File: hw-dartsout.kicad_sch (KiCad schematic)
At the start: 44 parts, among them J1 Conn_01x10_Socket, J2 Conn_01x10_Socket, J3 Conn_01x02_Pin, SW1 SW_Push, U1 ESP32-S3-WROOM-1, U3 NCP1117-3.3_SOT223

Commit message: First draft placement and layout
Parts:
- added J4: Conn_01x04_Pin, Connector_PinHeader_2.54mm:PinHeader_1x04_P2.54mm_Vertical, symbol Connector:Conn_01x04_Pin
- JP2: footprint Capacitor_SMD:C_0603_1608Metric -> Jumper:SolderJumper-3_P1.3mm_Bridged12_RoundedPad1.0x1.5mm
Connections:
- net +3V3: now also J4.1 (Pin_1)
- net ESP_RX: now also J4.3 (Pin_3)
- net ESP_TX: now also J4.2 (Pin_2)
- net GND: now also J4.4 (Pin_4)
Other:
- note added: "Add testpoints / leds WROOM or SOLO?? Office stock!"
- note removed: "Add testpoints / leds"
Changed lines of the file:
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@@
+    (stroke (width 0) (type default))
+  )
+  (wire (pts (xy 252.73 140.97) (xy 243.84 140.97))
     (stroke (width 0) (type default))
   )
@@
     (stroke (width 0) (type default))
   )
+  (wire (pts (xy 252.73 138.43) (xy 243.84 138.43))
+    (stroke (width 0) (type default))
+  )
   (wire (pts (xy 125.73 104.14) (xy 134.62 104.14))
     (stroke (width 0) (type default))
@@
     (stroke (width 0) (type default))
   )
+  (wire (pts (xy 254 143.51) (xy 243.84 143.51))
+    (stroke (width 0) (type default))
+  )
   (wire (pts (xy 134.62 73.66) (xy 125.73 73.66))
     (stroke (width 0) (type default))
@@
     (stroke (width 0) (type default))
   )
+  (wire (pts (xy 254 135.89) (xy 243.84 135.89))
+    (stroke (width 0) (type default))
+  )
   (wire (pts (xy 125.73 83.82) (xy 134.62 83.82))
     (stroke (width 0) (type default))
@@
     (effects (font (size 1.27 1.27)) (justify left bottom))
   )
-  (text "Add testpoints / leds" (at 176.53 170.18 0)
+  (text "Add testpoints / leds\nWROOM or SOLO?? Office stock!"
+    (at 179.07 172.72 0)
     (effects (font (size 1.27 1.27)) (justify left bottom))
   )
@@
     (effects (font (size 1.27 1.27)) (justify left bottom))
   )
+  (label "ESP_TX" (at 252.73 138.43 180) (fields_autoplaced)
+    (effects (font (size 1.27 1.27)) (justify right bottom))
+  )
   (label "ROW_10" (at 134.62 99.06 180) (fields_autoplaced)
     (effects (font (size 1.27 1.27)) (justify right bottom))
@@
   (label "ROW_05" (at 236.22 64.77 0) (fields_autoplaced)
     (effects (font (size 1.27 1.27)) (justify left bottom))
+  )
+  (label "ESP_RX" (at 252.73 140.97 180) (fields_autoplaced)
+    (effects (font (size 1.27 1.27)) (justify right bottom))
   )
   (label "ROW_07" (at 236.22 59.69 0) (fields_autoplaced)
@@
     )
   )
+  (symbol (lib_id "power:GND") (at 254 143.51 90) (unit 1)
+    (in_bom yes) (on_board yes) (dnp no) (fields_autoplaced)
+    (property "Reference" "#PWR018" (at 260.35 143.51 0)
+      (effects (font (size 1.27 1.27)) hide)
+    )
+    (property "Value" "GND" (at 257.81 143.51 90)
+      (effects (font (size 1.27 1.27)) (justify right))
+    )
+    (property "Footprint" "" (at 254 143.51 0)
+      (effects (font (size 1.27 1.27)) hide)
+    )
+    (property "Datasheet" "" (at 254 143.51 0)
+      (effects (font (size 1.27 1.27)) hide)
+    )
+    (pin "1")
+    (instances
+      (project "hw-dartsout"
+        (path "/c7fe45ce-d299-4ee8-a474-c3e52ad7951d"
+          (reference "#PWR018") (unit 1)
+        )
+      )
+    )
+  )
   (symbol (lib_id "Device:R") (at 198.12 83.82 0) (unit 1)
     (in_bom yes) (on_board yes) (dnp no)
@@
       (effects (font (size 1.27 1.27)))
     )
-    (property "Footprint" "Capacitor_SMD:C_0603_1608Metric" (at 260.35 99.06 0)
+    (property "Footprint" "Jumper:SolderJumper-3_P1.3mm_Bridged12_RoundedPad1.0x1.5mm" (at 260.35 99.06 0)
       (effects (font (size 1.27 1.27)) hide)
     )
@@
     )
   )
+  (symbol (lib_id "Connector:Conn_01x04_Pin") (at 238.76 138.43 0) (unit 1)
+    (in_bom yes) (on_board yes) (dnp no) (fields_autoplaced)
+    (property "Reference" "J4" (at 239.395 130.81 0)
+      (effects (font (size 1.27 1.27)))
+    )
+    (property "Value" "Conn_01x04_Pin" (at 239.395 133.35 0)
+      (effects (font (size 1.27 1.27)))
+    )
+    (property "Footprint" "Connector_PinHeader_2.54mm:PinHeader_1x04_P2.54mm_Vertical" (at 238.76 138.43 0)
+      (effects (font (size 1.27 1.27)) hide)
+    )
+    (property "Datasheet" "~" (at 238.76 138.43 0)
+      (effects (font (size 1.27 1.27)) hide)
+    )
+    (pin "4")
+    (pin "3")
+    (pin "2")
+    (pin "1")
+    (instances
+      (project "hw-dartsout"
+        (path "/c7fe45ce-d299-4ee8-a474-c3e52ad7951d"
+          (reference "J4") (unit 1)
+        )
+      )
+    )
+  )
   (symbol (lib_id "power:+5V") (at 50.8 167.64 0) (unit 1)
     (in_bom yes) (on_board yes) (dnp no)
@@
         )
       )
+    )
+  )
+  (symbol (lib_id "power:+3V3") (at 254 135.89 270) (unit 1)
+    (in_bom yes) (on_board yes) (dnp no) (fields_autoplaced)
+    (property "Reference" "#PWR019" (at 250.19 135.89 0)
+      (effects (font (size 1.27 1.27)) hide)
+    )
+    (property "Value" "+3V3" (at 257.81 135.89 90)
+      (effects (font (size 1.27 1.27)) (justify left))
+    )
+    (property "Footprint" "" (at 254 135.89 0)
+      (effects (font (size 1.27 1.27)) hide)
+    )
+    (property "Datasheet" "" (at 254 135.89 0)
+      (effects (font (size 1.27 1.27)) hide)
+    )
+    (pin "1")
+    (instances
+      (project "hw-dartsout"
+        (path "/c7fe45ce-d299-4ee8-a474-c3e52ad7951d"
+          (reference "#PWR019") (unit 1)
+        )
+      )

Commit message: PCB routed
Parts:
- removed TP2, TP3: TestPoint, TestPoint:TestPoint_Pad_D1.5mm, symbol Connector:TestPoint
- removed U1: ESP32-S3-WROOM-1, PCM_Espressif:ESP32-S3-WROOM-1, symbol PCM_Espressif:ESP32-S3-WROOM-1
- added J5, J6: Conn_01x10_Socket, Connector_PinSocket_2.54mm:PinSocket_1x10_P2.54mm_Vertical, symbol Connector:Conn_01x10_Socket
- added TP6: TestPoint, TestPoint:TestPoint_Pad_D1.5mm, symbol Connector:TestPoint
- added U1: ESP32-S2-SOLO, PCM_Espressif:ESP32-S2-SOLO, symbol guille-lib:ESP32-S2-SOLO
- H1, H2, H3, H4: footprint MountingHole:MountingHole_3.2mm_M3_Pad_TopBottom -> MountingHole:MountingHole_3.2mm_M3_DIN965_Pad_TopBottom
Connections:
- net +3V3: now also U1.2 (3V3)
- net COL_01: now also J5.1 (Pin_1), U1.30 (SPIDQS/GPIO37/FSPIQ)
- net COL_02: now also J5.2 (Pin_2), U1.29 (SPIIO7/GPIO36/FSPICLK)
- net COL_03: now also J5.3 (Pin_3), U1.28 (SPIIO6/GPIO35/FSPID)
- net COL_04: now also J5.4 (Pin_4), U1.25 (SPIIO5/GPIO34/FSPICS0)
- net COL_05: now also J5.5 (Pin_5), U1.24 (SPIIO4/GPIO33/FSPIHD)
- net COL_06: now also J5.6 (Pin_6), U1.23 (GPIO21)
- net COL_07: now also J5.7 (Pin_7), U1.22 (GPIO14/TOUCH14/ADC2_CH3/FSPIWP/FSPIDQS)
- net COL_08: now also J5.8 (Pin_8), U1.21 (GPIO13/TOUCH13/ADC2_CH2/FSPIQ/FSPIIO7)
- net COL_09: now also J5.9 (Pin_9), U1.20 (GPIO12/TOUCH12/ADC2_CH1/FSPICLK/FSPIIO6)
- net COL_10: now also J5.10 (Pin_10), U1.19 (GPIO11/TOUCH11/ADC2_CH0/FSPID/FSPIIO5)
- net ESP_IO0: now also U1.27 (GPIO0)
- net ESP_RX: now also U1.36 (U0RXD/GPIO44/CLK_OUT2)
- net ESP_TX: now also U1.37 (U0TXD/GPIO43/CLK_OUT1)
- net GND: now also U1.1 (GND), U1.40 (GND), U1.41 (GND)
- net ROW_01: now also J6.1 (Pin_1), U1.18 (GPIO10/TOUCH10/ADC1_CH9/FSPICS0/FSPIIO4)
- net ROW_02: now also J6.2 (Pin_2), U1.17 (GPIO9/TOUCH9/ADC1_CH8/FSPIHD)
- net ROW_03: now also J6.3 (Pin_3), U1.15 (GPIO3/TOUCH3/ADC1_CH2)
- net ROW_04: now also J6.4 (Pin_4), U1.12 (GPIO8/TOUCH8/ADC1_CH7)
- net ROW_05: now also J6.5 (Pin_5), U1.11 (GPIO18/U1RXD/ADC2_CH7/DAC_2/CLK_OUT3)
- net ROW_06: now also J6.6 (Pin_6), U1.10 (GPIO17/U1TXD/ADC2_CH6/DAC_1)
- net ROW_07: now also J6.7 (Pin_7), U1.7 (GPIO7/TOUCH7/ADC1_CH6)
- net ROW_08: now also J6.8 (Pin_8), U1.6 (GPIO6/TOUCH6/ADC1_CH5)
- net ROW_09: now also J6.9 (Pin_9), U1.5 (GPIO5/TOUCH5/ADC1_CH4)
- net ROW_10: now also J6.10 (Pin_10), U1.4 (GPIO4/TOUCH4/ADC1_CH3)
- net at TP5.1: now also U1.16 (GPIO46)
- net at TP4.1: now also U1.38 (GPIO2/TOUCH2/ADC1_CH1)
- net at C5.1, R21.2: now also U1.3 (EN)
- net at TP1.1: now also U1.39 (GPIO1/TOUCH1/ADC1_CH0)
- new net: TP6.1, U1.31 (GPIO38/FSPIWP)
- no-connect marks 12 -> 13
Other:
- note added: "Add testpoints / leds WROOM or SOLO?? Office stock! Separar headers (ocupan 1 hole de mas, separar 2.54*3) En prototipo, están separados 2.54 * 8"
- note removed: "Add testpoints / leds WROOM or SOLO?? Office stock!"
- moved on the sheet: C5, J1, J2, JP1, JP2, R1, R10, R11, R12, R13, R14, R15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

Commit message: Finish route, serigrphy and checks
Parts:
- added D1, D2, D3: LED, LED_SMD:LED_0603_1608Metric, symbol Device:LED
- added R23, R24, R25: 1k, Resistor_SMD:R_0603_1608Metric, symbol Device:R
- R1, R10, R11, R12, R13, R14, R15, R16, R17, R18, R19, R2, R20, R3, R4, R5, R6, R7, R8, R9: value R -> 10k
- renumbered C4 to C3, C3 to C4, H2 to H1, H1 to H2, TP5 to TP1, TP1 to TP2, TP6 to TP3, U3 to U2
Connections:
- net +3V3: now also D1.2 (A)
- net GND: now also R23.2, R24.2, R25.2
- net LED2: now reaches TP4.1, U1.38 (GPIO2/TOUCH2/ADC1_CH1)
- net LED2: now also D3.2 (A)
- net LED1: now reaches TP2.1, U1.39 (GPIO1/TOUCH1/ADC1_CH0)
- net LED1: now also D2.2 (A)
- new net: D3.1 (K), R25.1
- new net: D2.1 (K), R24.1
- new net: D1.1 (K), R23.1
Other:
- moved on the sheet: C1, C2, C3, C4, C5, H1, H2, H3, H4, J3, J4, R21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

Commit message: Revision 0.1
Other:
- note removed: "Add testpoints / leds WROOM or SOLO?? Office stock! Separar headers (ocupan 1 hole de mas, separar 2.54*3) En prototipo, están separados 2.54 * 8"
- company: (none) -> Guille González
- title: (none) -> Dartsout
- moved on the sheet: D1, D2, D3, H1, H2, H3, H4, J1, J2, J4, J5, J6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

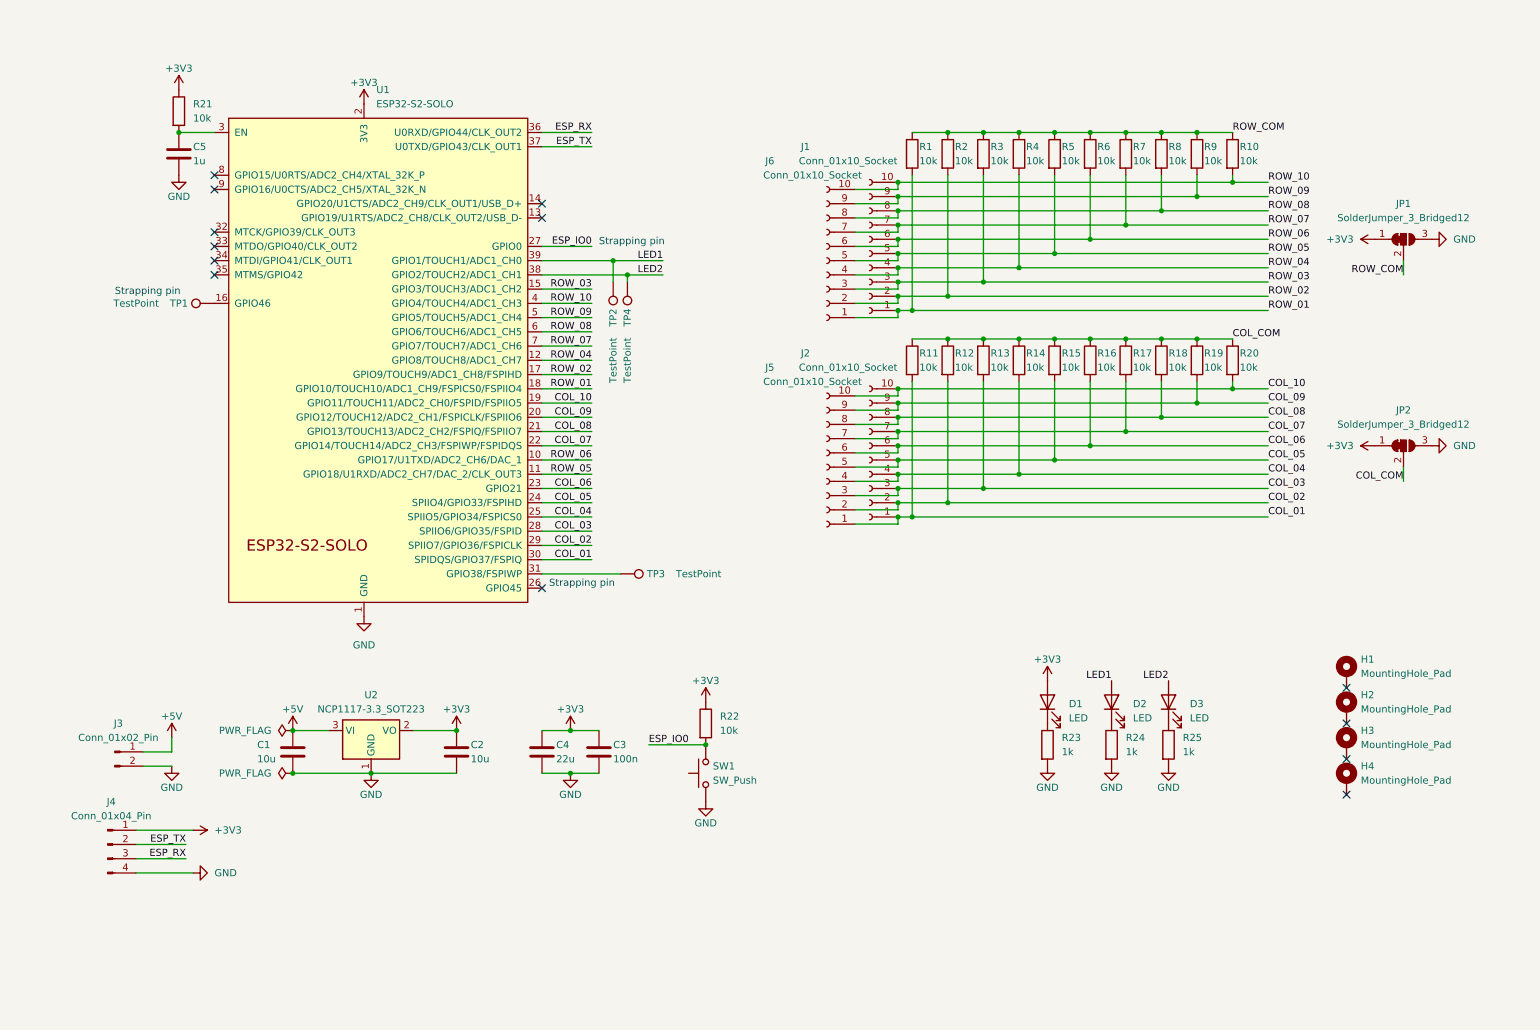
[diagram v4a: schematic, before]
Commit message: Changed sch and start with layout for next version
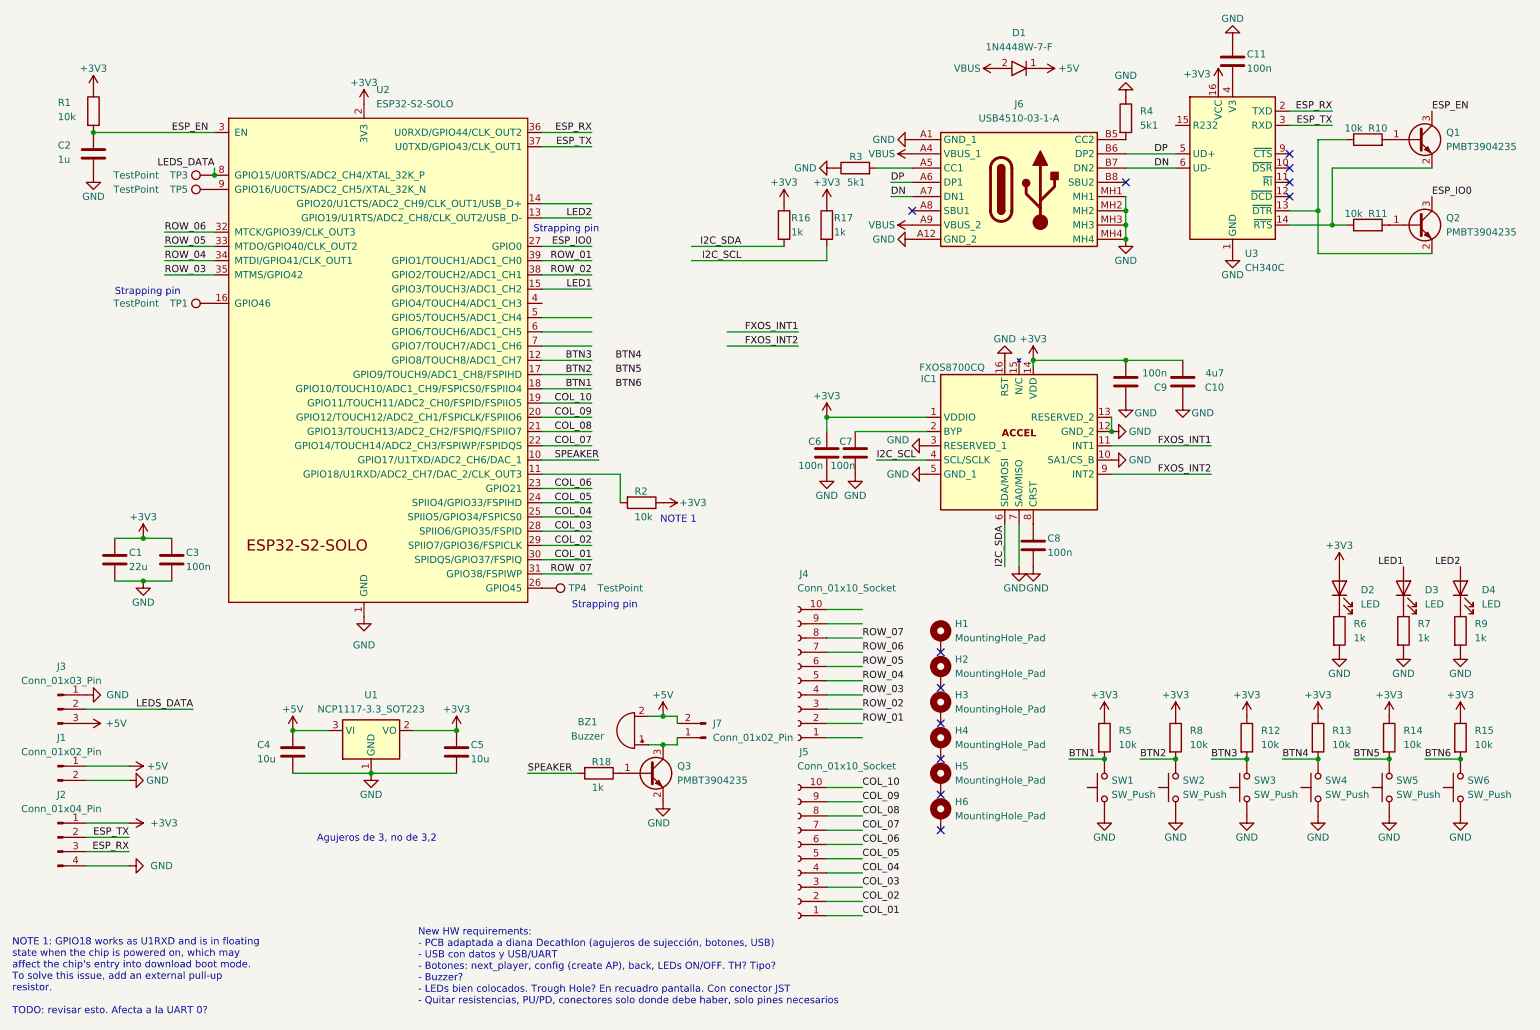
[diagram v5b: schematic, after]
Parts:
- removed J4: Conn_01x04_Pin, Connector_PinHeader_2.54mm:PinHeader_1x04_P2.54mm_Vertical, symbol Connector:Conn_01x04_Pin
- removed J5, J6: Conn_01x10_Socket, Connector_PinSocket_2.54mm:PinSocket_1x10_P2.54mm_Vertical, symbol Connector:Conn_01x10_Socket
- removed JP1, JP2: SolderJumper_3_Bridged12, Jumper:SolderJumper-3_P1.3mm_Bridged12_RoundedPad1.0x1.5mm, symbol Jumper:SolderJumper_3_Bridged12
- removed R1, R19, R20, R22, R6, R7, R9: 10k, Resistor_SMD:R_0603_1608Metric, symbol Device:R
- removed TP2: TestPoint, TestPoint:TestPoint_Pad_D1.5mm, symbol Connector:TestPoint
- added BZ1: Buzzer, Buzzer_Beeper:Buzzer_12x9.5RM7.6, symbol Device:Buzzer
- added C10: 4u7, Capacitor_SMD:C_0805_2012Metric, symbol Device:C
- added C11, C6, C7, C8, C9: 100n, Capacitor_SMD:C_0603_1608Metric, symbol Device:C
- added D1: 1N4448W-7-F, Diode_SMD:D_SOD-123, symbol guille-lib:1N4448W-7-F
- added H1, H2: MountingHole_Pad, MountingHole:MountingHole_3.2mm_M3_DIN965_Pad_TopBottom, symbol Mechanical:MountingHole_Pad
- added IC1: FXOS8700CQ, guille-lib:FXOS8700CQ, symbol guille-lib:FXOS8700CQ
- added J2: Conn_01x04_Pin, Connector_PinHeader_2.54mm:PinHeader_1x04_P2.54mm_Vertical, symbol Connector:Conn_01x04_Pin
- added J3: Conn_01x03_Pin, Connector_JST:JST_XH_B3B-XH-A_1x03_P2.50mm_Vertical, symbol Connector:Conn_01x03_Pin
- added J6: USB4510-03-1-A, guille-lib:USB4510031A, symbol guille-lib:USB4510-03-1-A
- added J7: Conn_01x02_Pin, Connector_PinHeader_2.54mm:PinHeader_1x02_P2.54mm_Horizontal, symbol Connector:Conn_01x02_Pin
- added Q1, Q2, Q3: PMBT3904235, Package_TO_SOT_SMD:SOT-23, symbol guille-lib:PMBT3904235
- added SW2, SW3, SW4, SW5, SW6: SW_Push, guille-lib:SW_SPST_PTS810, symbol guille-lib:PTS810
- added TP5: TestPoint, TestPoint:TestPoint_Pad_D1.5mm, symbol Connector:TestPoint
- added U3: CH340C, Package_SO:SOIC-16_3.9x9.9mm_P1.27mm, symbol Interface_USB:CH340C
- R16, R17, R18: value 10k -> 1k
- R3, R4: value 10k -> 5k1
- U2: renamed from U1; footprint PCM_Espressif:ESP32-S2-SOLO -> guille-lib:ESP32-S2-SOLO
- renumbered C4 to C1, C5 to C2, C1 to C4, C2 to C5, D1 to D2, D2 to D3, D3 to D4, H1 to H3, H2 to H4, H3 to H5, H4 to H6, J3 to J1, J1 to J4, J2 to J5, R21 to R1, R23 to R6, R24 to R7, R25 to R9, U2 to U1
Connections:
- net +3V3: now also R12.1, R13.1, R14.1, R15.1, R16.1, R17.1, R2.1, R5.1, R8.1, C10.2, C6.1, C9.2, IC1.1 (VDDIO), IC1.14 (VDD), J2.1 (Pin_1), U3.16 (VCC)
- net +5V: now also BZ1.2 (-), D1.1, J3.3 (Pin_3), J7.2 (Pin_2)
- net COL_01: no longer R11.2
- net COL_02: no longer R12.2
- net COL_03: no longer R13.2
- net COL_04: no longer R14.2
- net COL_05: no longer R15.2
- net COL_06: no longer R16.2
- net COL_07: no longer R17.2
- net COL_08: no longer R18.2
- net ESP_IO0: now also Q2.3; no longer SW1.2
- net ESP_RX: now also J2.3 (Pin_3), U3.2 (TXD)
- net ESP_TX: now also J2.2 (Pin_2), U3.3 (RXD)
- net GND: now also R3.1, R4.1, C10.1, C11.1, C6.2, C7.1, C8.2, C9.1, IC1.10 (SA1/CS_B), IC1.12 (GND_2), IC1.13 (RESERVED_2), IC1.16 (RST), IC1.3 (RESERVED_1), IC1.5 (GND_1), IC1.7 (SA0/MISO), J2.4 (Pin_4), J3.1 (Pin_1), J6.A1 (GND_1), J6.A12 (GND_2), J6.MH1, J6.MH2, J6.MH3, J6.MH4, Q3.2, SW2.1, SW3.1, SW4.1, SW5.1, SW6.1, U3.1 (GND)
- net LED1: now also U2.15 (GPIO3/TOUCH3/ADC1_CH2); no longer U2.39 (GPIO1/TOUCH1/ADC1_CH0)
- net LED2: now also U2.13 (GPIO19/U1RTS/ADC2_CH8/CLK_OUT2/USB_D-); no longer TP4.1, U2.38 (GPIO2/TOUCH2/ADC1_CH1)
- net ROW_01: now also J4.2 (Pin_2), U2.39 (GPIO1/TOUCH1/ADC1_CH0); no longer J4.1 (Pin_1), U2.18 (GPIO10/TOUCH10/ADC1_CH9/FSPICS0/FSPIIO4)
- net ROW_02: now also J4.3 (Pin_3), U2.38 (GPIO2/TOUCH2/ADC1_CH1); no longer J4.2 (Pin_2), R2.2, U2.17 (GPIO9/TOUCH9/ADC1_CH8/FSPIHD)
- net ROW_03: now also J4.4 (Pin_4), U2.35 (MTMS/GPIO42); no longer J4.3 (Pin_3), R3.2, U2.15 (GPIO3/TOUCH3/ADC1_CH2)
- net ROW_04: now also J4.5 (Pin_5), U2.34 (MTDI/GPIO41/CLK_OUT1); no longer J4.4 (Pin_4), R4.2, U2.12 (GPIO8/TOUCH8/ADC1_CH7)
- net ROW_05: now also J4.6 (Pin_6), U2.33 (MTDO/GPIO40/CLK_OUT2); no longer J4.5 (Pin_5), R5.2, U2.11 (GPIO18/U1RXD/ADC2_CH7/DAC_2/CLK_OUT3)
- net ROW_06: now also J4.7 (Pin_7), U2.32 (MTCK/GPIO39/CLK_OUT3); no longer J4.6 (Pin_6), U2.10 (GPIO17/U1TXD/ADC2_CH6/DAC_1)
- net ROW_07: now also J4.8 (Pin_8), U2.31 (GPIO38/FSPIWP); no longer J4.7 (Pin_7), U2.7 (GPIO7/TOUCH7/ADC1_CH6)
- net at U2.26 (GPIO45): now also TP4.1
- net ESP_EN: now reaches C2.1, R1.2, U2.3 (EN)
- net ESP_EN: now also Q1.3
- net LEDS_DATA: now reaches TP3.1
- net LEDS_DATA: now also U2.8 (GPIO15/U0RTS/ADC2_CH4/XTAL_32K_P), J3.2 (Pin_2); no longer U2.31 (GPIO38/FSPIWP)
- net at U2.9 (GPIO16/U0CTS/ADC2_CH5/XTAL_32K_N): now also TP5.1
- removed net COL_COM: R11.1, R12.1, R13.1, R14.1, R15.1, R16.1, R17.1, R18.1
- removed net ROW_08: J4.8 (Pin_8), R8.2, U2.6 (GPIO6/TOUCH6/ADC1_CH5)
- net ROW_09: no longer names the net of U2.5 (GPIO5/TOUCH5/ADC1_CH4)
- net ROW_09: no longer J4.9 (Pin_9)
- removed net ROW_10: J4.10 (Pin_10), R10.2, U2.4 (GPIO4/TOUCH4/ADC1_CH3)
- removed net ROW_COM: R10.1, R2.1, R3.1, R4.1, R5.1, R8.1
- new net: Q3.1, R18.1
- new net: J6.A5 (CC1), R3.2
- new net: J6.B5 (CC2), R4.2
- new net: Q1.1, R10.2
- new net: Q1.2, R11.1, U3.14 (~{RTS})
- new net: R2.2, U2.11 (GPIO18/U1RXD/ADC2_CH7/DAC_2/CLK_OUT3)
- new net: C11.2, U3.4 (V3)
- new net: Q2.1, R11.2
- new net: Q2.2, R10.1, U3.13 (~{DTR})
- new net: C7.2, IC1.2 (BYP)
- new net: C8.1, IC1.8 (CRST)
- new net: BZ1.1 (+), J7.1 (Pin_1), Q3.3
- new net BTN1: R5.2, SW1.2, U2.18 (GPIO10/TOUCH10/ADC1_CH9/FSPICS0/FSPIIO4)
- new net BTN2: R8.2, SW2.2, U2.17 (GPIO9/TOUCH9/ADC1_CH8/FSPIHD)
- new net BTN3: R12.2, SW3.2, U2.12 (GPIO8/TOUCH8/ADC1_CH7)
- new net BTN4: R13.2, SW4.2
- new net BTN5: R14.2, SW5.2
- new net BTN6: R15.2, SW6.2
- new net DN: J6.A7 (DN1), J6.B7 (DN2), U3.6 (UD-)
- new net DP: J6.A6 (DP1), J6.B6 (DP2), U3.5 (UD+)
- new net FXOS_INT1: IC1.11 (INT1)
- new net FXOS_INT2: IC1.9 (INT2)
- new net I2C_SCL: IC1.4 (SCL/SCLK), R17.2
- new net I2C_SDA: IC1.6 (SDA/MOSI), R16.2
- new net SPEAKER: R18.2, U2.10 (GPIO17/U1TXD/ADC2_CH6/DAC_1)
- new net VBUS: D1.2, J6.A4 (VBUS_1), J6.A9 (VBUS_2)
- no-connect marks 13 -> 12
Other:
- note added: "Agujeros de 3, no de 3,2"
- note added: "NOTE 1"
- note added: "NOTE 1: GPIO18 works as U1RXD and is in floating state when the chip is powered on, which may affect the chip's entry into download boot mode. To solve this issue, add an external pull-up resistor. TODO: revisar esto. Afecta a la UART 0?"
- note added: "New HW requirements: - PCB adaptada a diana Decathlon (agujeros de sujección, botones, USB) - USB con datos y USB/UART - Botones: next_player, config (create AP), back, LEDs ON/OFF. TH? Tipo? - Buzzer? - LEDs bien colocados. Trough Hole? En recuadro pantalla. Con conector JST - Quitar resistencias, PU/PD, conectores solo donde debe haber, solo pines necesarios"
- moved on the sheet: C1, C2, C3, D2, D3, D4, H3, H4, H5, H6, J1, J4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
